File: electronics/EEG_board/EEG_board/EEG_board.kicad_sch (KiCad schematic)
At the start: 121 parts, among them J1 HDR-2x1, J10 HDR-2x1, J11 HDR-2x1, J15 HDR-4x1, J16 ON OFF, J17 HDR-4x1, J18 HDR-4x1, J2 HDR-2x1, J20 Conn_02x03_Counter_Clockwise, J21 Conn_02x03_Counter_Clockwise, J22 Conn_02x04_Counter_Clockwise, J23 HDR-4x1, J24 Conn_01x03, J25 ON OFF, J26 HDR-2x1, J27 HDR-2x1, J28 HDR-2x1, J29 HDR-3x1, J3 HDR-2x1, J30 HDR-3x1, J31 HDR-3x1, J7 HDR-4x1, J8 HDR-2x1, J9 HDR-2x1, U17 AP2112K-3.3, U18 Teensy4.1, U19 ADS1299-4PAG, U20 MEA1D, U21 TCA9548APWR, U22 TPS730, U23 TPS72325DBV, U56 OPA376xxDBV, U57 OPA376xxDBV

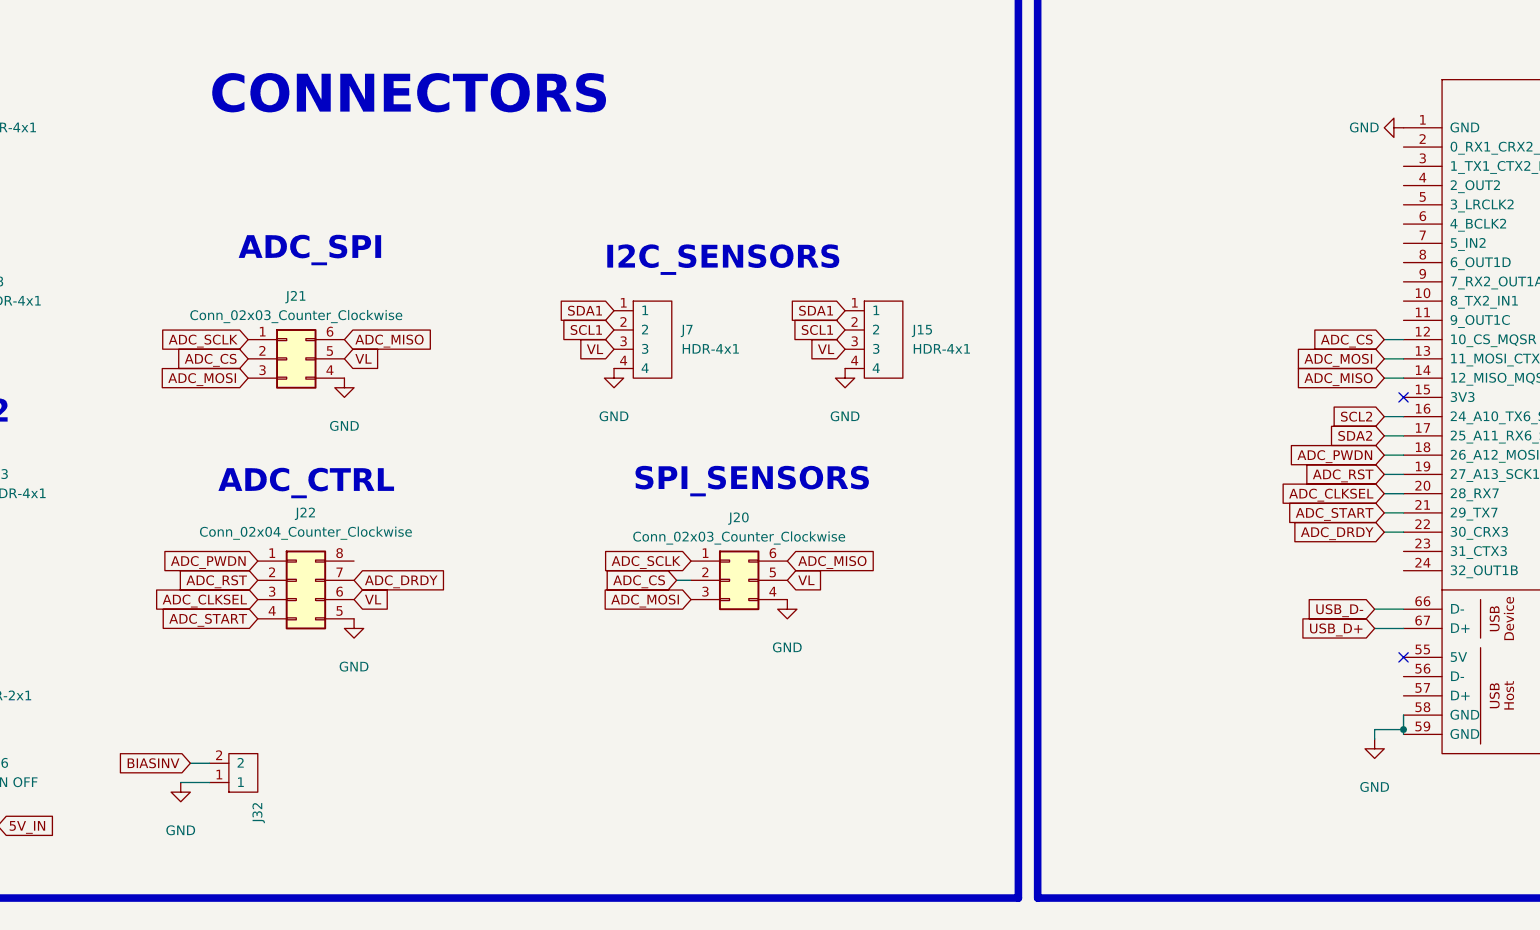
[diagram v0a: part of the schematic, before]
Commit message: working on gui adding accel review
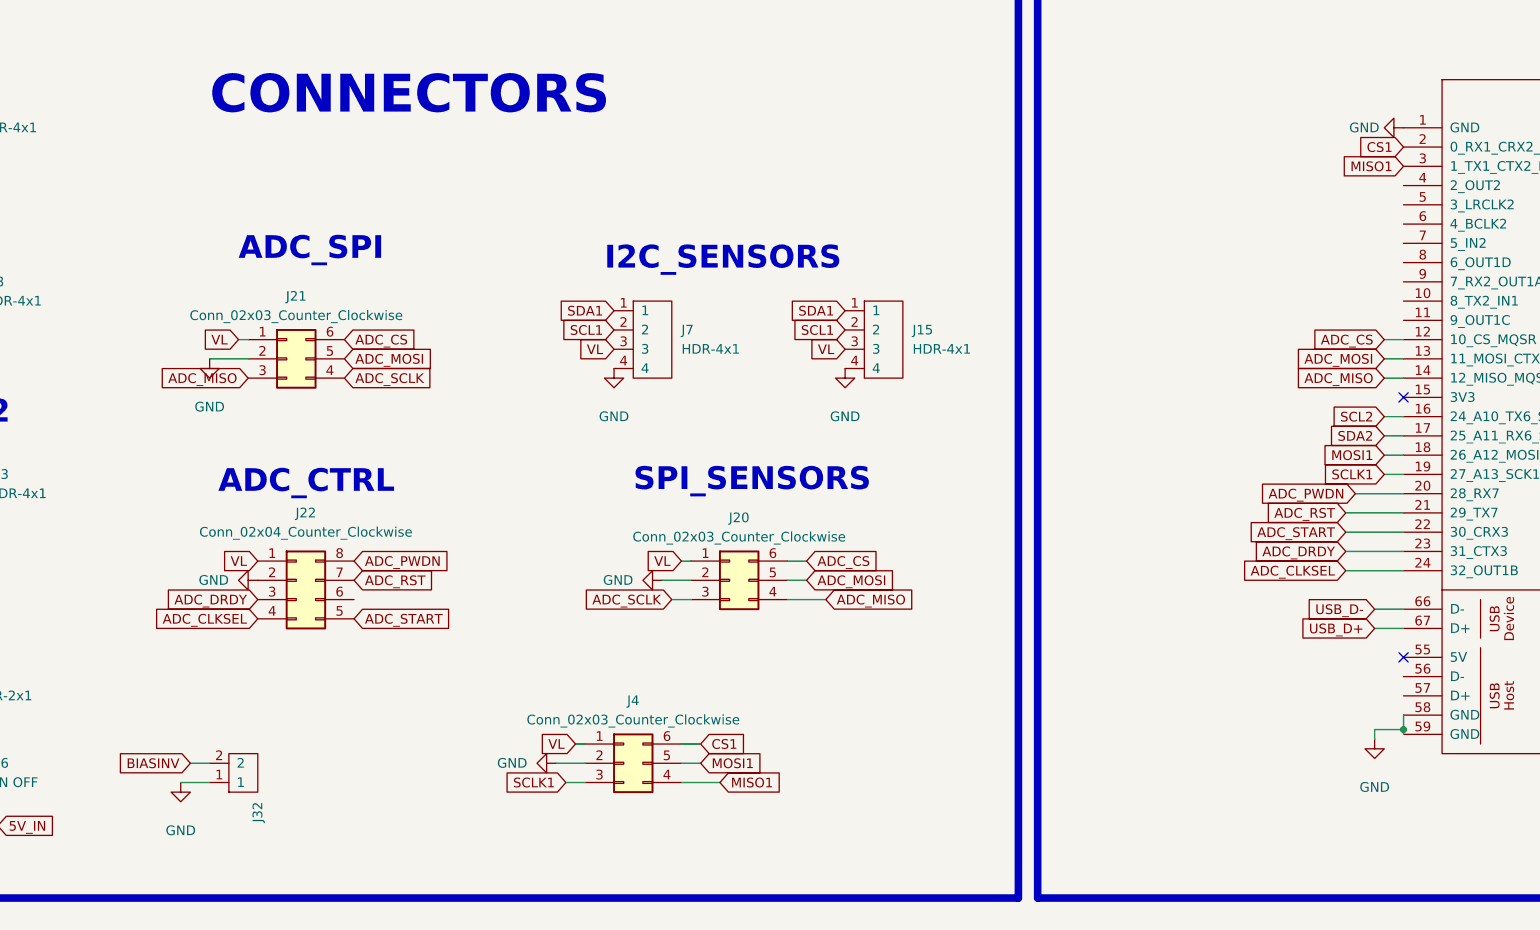
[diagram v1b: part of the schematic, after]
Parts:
- added J4: Conn_02x03_Counter_Clockwise, Connector_PinHeader_2.54mm:PinHeader_2x03_P2.54mm_Vertical, symbol Connector_Generic:Conn_02x03_Counter_Clockwise
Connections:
- net ADC_CLKSEL: now also J22.4 (Pin_4), U18.24 (32_OUT1B); no longer J22.3 (Pin_3), U18.20 (28_RX7)
- net ADC_CS: now also J20.6 (Pin_6), J21.6 (Pin_6); no longer J20.2 (Pin_2), J21.2 (Pin_2)
- net ADC_DRDY: now also J22.3 (Pin_3), U18.23 (31_CTX3); no longer J22.7 (Pin_7), U18.22 (30_CRX3)
- net ADC_MISO: now also J20.4 (Pin_4), J21.3 (Pin_3); no longer J20.6 (Pin_6), J21.6 (Pin_6)
- net ADC_MOSI: now also J20.5 (Pin_5), J21.5 (Pin_5); no longer J20.3 (Pin_3), J21.3 (Pin_3)
- net ADC_PWDN: now also J22.8 (Pin_8), U18.20 (28_RX7); no longer J22.1 (Pin_1), U18.18 (26_A12_MOSI1)
- net ADC_RST: now also J22.7 (Pin_7), U18.21 (29_TX7); no longer J22.2 (Pin_2), U18.19 (27_A13_SCK1)
- net ADC_SCLK: now also J20.3 (Pin_3), J21.4 (Pin_4); no longer J20.1 (Pin_1), J21.1 (Pin_1)
- net ADC_START: now also J22.5 (Pin_5), U18.22 (30_CRX3); no longer J22.4 (Pin_4), U18.21 (29_TX7)
- net GND: now also J20.2 (Pin_2), J21.2 (Pin_2), J22.2 (Pin_2), J4.2 (Pin_2); no longer J20.4 (Pin_4), J21.4 (Pin_4), J22.5 (Pin_5)
- net VL: now also J20.1 (Pin_1), J21.1 (Pin_1), J22.1 (Pin_1), J4.1 (Pin_1); no longer J20.5 (Pin_5), J21.5 (Pin_5), J22.6 (Pin_6)
- net CS1: now reaches U18.2 (0_RX1_CRX2_CS1)
- net CS1: now also J4.6 (Pin_6)
- net MISO1: now reaches U18.3 (1_TX1_CTX2_MISO1)
- net MISO1: now also J4.4 (Pin_4)
- new net MOSI1: J4.5 (Pin_5), U18.18 (26_A12_MOSI1)
- new net SCLK1: J4.3 (Pin_3), U18.19 (27_A13_SCK1)

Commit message: implementing down sampling
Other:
- note added: "BIAS"
- note added: "I2C multiplexer"
- note added: "Signal Conditioning Channels"
